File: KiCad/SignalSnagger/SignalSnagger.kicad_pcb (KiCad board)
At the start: 4 copper layers, 133.4 x 44.3 mm, 180 parts, among them J102 Left, J104 Right, J105 36-5005-ND, J106 36-5006-ND, J107 36-5006-ND, J108 36-5005-ND, J109 36-5006-ND, J110 36-5006-ND, J203 Conn_01x02, J204 Conn_01x02, J301 35RASMT2BHSNTRX, J302 36-5005-ND, J303 36-5005-ND, J304 36-5006-ND, P201 ISP/PDI, Q101 MMBT2222A, Q102 MMBT2222A, Q103 MMBT2222A, Q104 MMBT2222A, Q105 MMBT2222A, Q201 BSS84W-7-F, Q202 BSS138W-7-F, SW201 SW_SPST, SW202 SW_SPST, SW203 PEC12R-4225F-S0024, T101 Transformer_1P_SS, U102 QS3253QG8, U103 REF4132B33, U104 DG9422E, U105 DG9422E, U201 AVR128DA48, U202 SI5351, U203 LP2985-5.0, U204 LP2985-3.3, U205 EA_DOGS104W-A, U206 LP2985-5.0, U207 MAX1683EUK, U302 TS912IDT, U303 TS912IDT, U304 LM386, X201 ECS-327TXO-30-TR, X202 25 MHz

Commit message: Ver 0.307
PCB updates
o All components are now placed onto the board with not traces drawn
 oRe-added the stereo channel. Parts are numbered starting with 901, so they can be easily identified for not populating or future removal
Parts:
- removed U303: TS912IDT, Package_SO:SO-8_3.9x4.9mm_P1.27mm
- added C901: 150nF, Capacitor_SMD:C_0603_1608Metric, F.Cu at (166.2, 97.8)
- added C902: 4.7nF, Capacitor_SMD:C_0603_1608Metric, F.Cu at (161.8, 96.0)
- added C903: 100nF, Capacitor_SMD:C_0603_1608Metric, F.Cu at (161.8, 97.5)
- added C906: 10nF, Capacitor_SMD:C_0603_1608Metric, F.Cu at (201.4, 107.2)
- added C907: 47uF, Capacitor_SMD:C_1210_3225Metric, F.Cu at (200.6, 101.1)
- added C908: 1uF, Capacitor_SMD:C_0603_1608Metric, F.Cu at (202.2, 109.7)
- added C909: 100nF, Capacitor_SMD:C_0603_1608Metric, F.Cu at (201.2, 103.6)
- added C910: 10uF, Capacitor_SMD:C_0603_1608Metric, F.Cu at (201.4, 105.7)
- added C911: 100nF, Capacitor_SMD:C_0603_1608Metric, F.Cu at (209.2, 103.2)
- added C912: 22uF, Capacitor_SMD:C_0805_2012Metric, F.Cu at (208.3, 100.6)
- added R901: 4.7k, Resistor_SMD:R_0603_1608Metric, F.Cu at (169.3, 96.4)
- added R902: 7.5k, Resistor_SMD:R_0603_1608Metric, F.Cu at (167.7, 97.9)
- added R903: 51k, Resistor_SMD:R_0603_1608Metric, F.Cu at (157.0, 99.7)
- added R907: 10k, Resistor_SMD:R_0603_1608Metric, F.Cu at (196.5, 106.9)
- added R909: 10, Resistor_SMD:R_0603_1608Metric, F.Cu at (198.2, 103.5)
- added R910: 470, Resistor_SMD:R_0603_1608Metric, F.Cu at (200.6, 109.7)
- added R911: 10, Resistor_SMD:R_0603_1608Metric, F.Cu at (209.2, 106.3)
- added RV901: 100k, Potentiometer_SMD:Potentiometer_Bourns_TC33X_Vertical, F.Cu at (189.0, 105.3)
- added TP901: Conn_01x03, Connector_PinHeader_2.54mm:PinHeader_1x03_P2.54mm_Vertical, F.Cu at (192.8, 102.0)
- added U901: TS912IDT, Package_SO:SO-8_3.9x4.9mm_P1.27mm, F.Cu at (155.8, 94.8)
- added U902: LM386, Package_SO:SO-8_3.9x4.9mm_P1.27mm, F.Cu at (205.7, 106.4)
- JP103, JP104, JP105, JP106, JP107: footprint Jumper:Jumper_THT_1x02_P1.27mm_Vertical -> Jumper:Jumper_THT-1x02_Bridged_Circular
- moved R205 87.1 mm to (184.4, 85.4)
- moved J204 85.9 mm to (187.8, 84.7), turned to 180 degrees
- moved D204 85.5 mm to (191.4, 85.2)
- moved D203 84.7 mm to (191.3, 79.4)
- moved R204 83.9 mm to (184.1, 83.7)
- moved C202 83.9 mm to (168.8, 85.2)
- moved C217 83.9 mm to (167.4, 80.7)
- moved U201 83.9 mm to (175.6, 85.5)
- moved X201 83.9 mm to (172.9, 77.7)
- moved C213 83.9 mm to (176.8, 78.5)
- moved C214 83.9 mm to (184.0, 81.0)
- moved C221 83.9 mm to (170.1, 77.2)
- moved L201 83.9 mm to (180.7, 79.3)
- moved R209 83.9 mm to (180.9, 81.0)
- moved C203 83.9 mm to (178.4, 78.5)
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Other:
- board text added: "Sense Adjust"
- board text removed: "JP105"
- board text removed: "Sense"

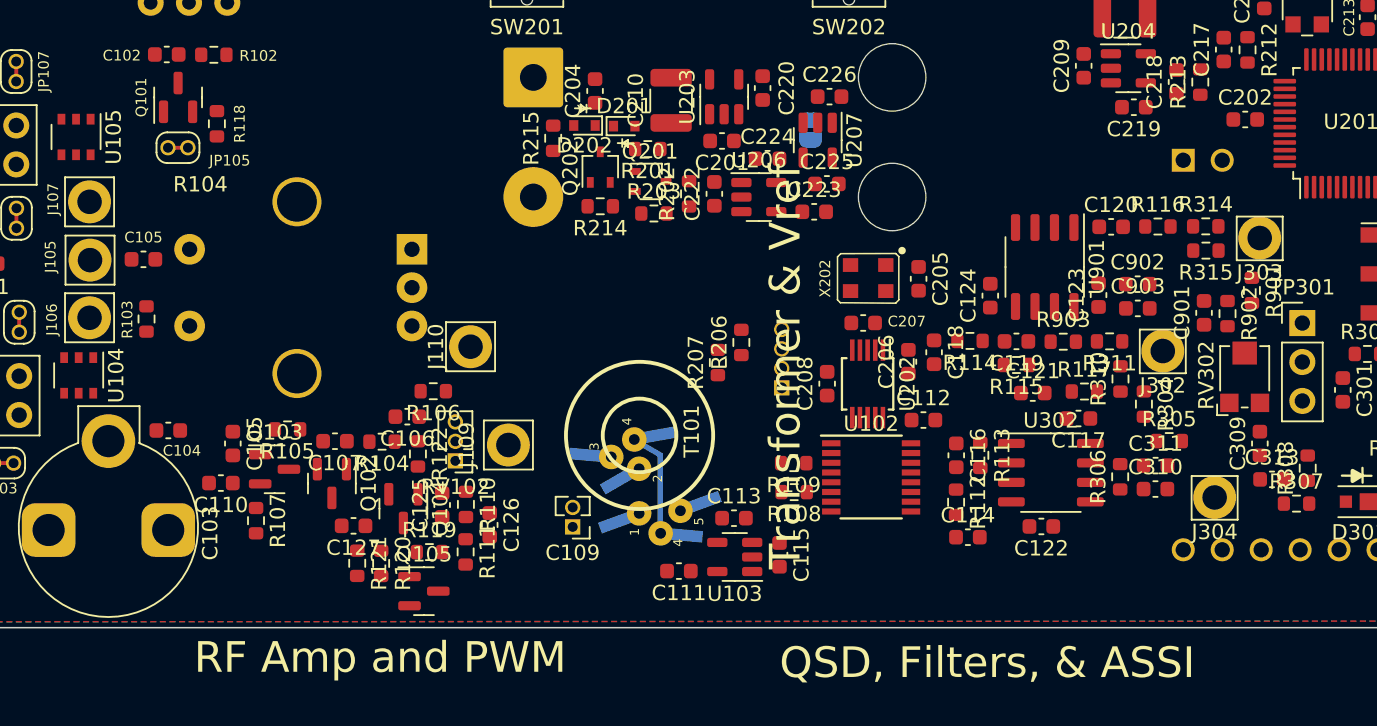
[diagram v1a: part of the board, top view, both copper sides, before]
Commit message: Ver 0.308
Schematic and PCB tweaks
Set board thickness to 1.6mm
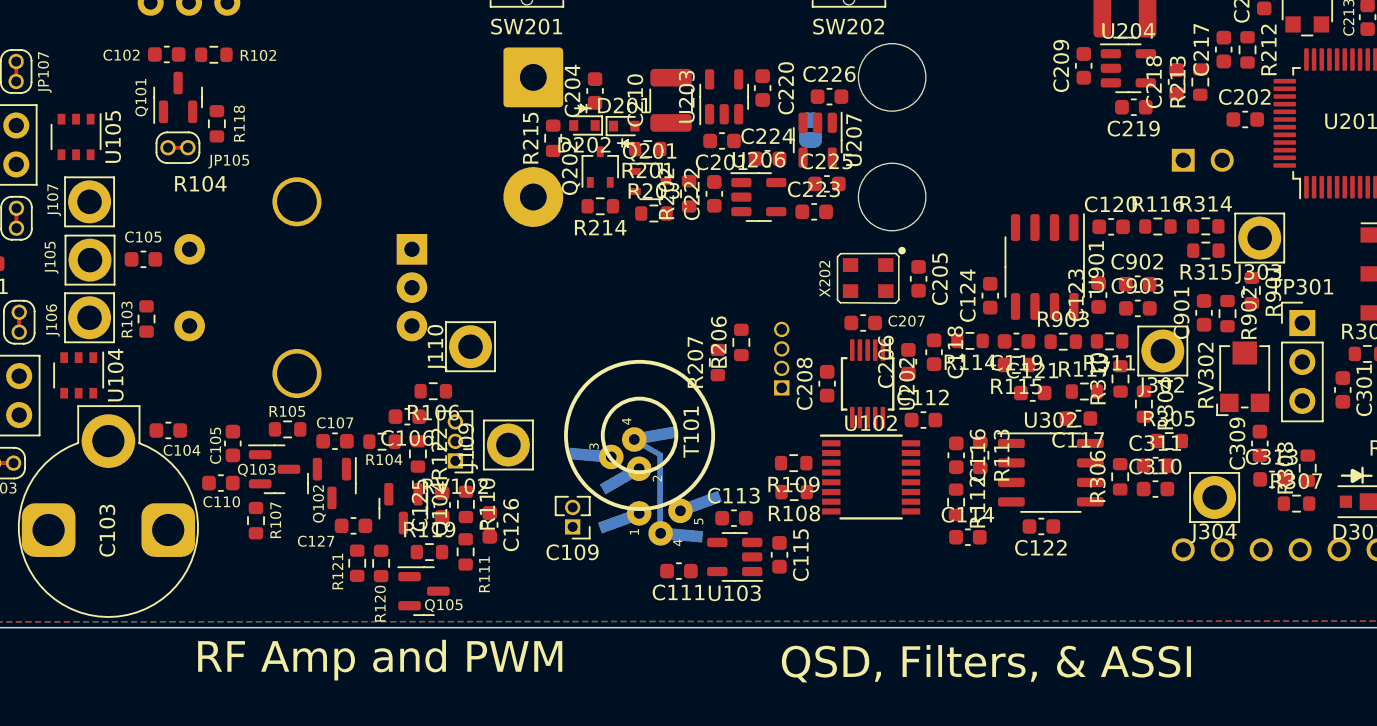
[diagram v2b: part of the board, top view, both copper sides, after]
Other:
- board text removed: "Transformer & Vref"

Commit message: Ver 0.309
PCB layout updates
Schematic updates
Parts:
- removed J303: 36-5005-ND, Connector_Pin:Pin_D1.6mm_L8.5mm_W2.8mm_FlatFork
- removed R116: 100, Resistor_SMD:R_0603_1608Metric
- added C108: 100nF, Capacitor_SMD:C_0603_1608Metric, F.Cu at (92.2, 88.8)
- added C118: 100nF, Capacitor_SMD:C_0603_1608Metric, F.Cu at (92.3, 103.2)
- added J218: Conn_01x02, Connector_PinSocket_1.27mm:PinSocket_1x02_P1.27mm_Vertical, F.Cu at (127.9, 75.5)
- added J219: Conn_01x02, Connector_PinSocket_1.27mm:PinSocket_1x02_P1.27mm_Vertical, F.Cu at (148.9, 75.5)
- added J220: Conn_01x02, Connector_PinSocket_1.27mm:PinSocket_1x02_P1.27mm_Vertical, F.Cu at (127.9, 115.5)
- added J221: Conn_01x02, Connector_PinSocket_1.27mm:PinSocket_1x02_P1.27mm_Vertical, F.Cu at (148.9, 115.4)
- added J903: 36-5005-ND, Connector_Pin:Pin_D1.6mm_L8.5mm_W2.8mm_FlatFork, F.Cu at (161.8, 105.6)
- added R916: 100, Resistor_SMD:R_0603_1608Metric, F.Cu at (156.9, 103.9)
- added SW204: SW_SPST, Button_Switch_SMD:SW_SPST_TL1014BF160QG, F.Cu at (122.1, 116.4)
- added SW205: SW_SPST, Button_Switch_SMD:SW_SPST_TL1014BF160QG, F.Cu at (143.1, 116.3)
- C103: moved to B.Cu
- C109: footprint Connector_PinHeader_1.27mm:PinHeader_1x02_P1.27mm_Vertical -> Capacitor_SMD:C_0603_1608Metric
- J102: renamed from J104; value Right -> Left; moved to B.Cu
- J104: renamed from J102; value Left -> Right; moved to B.Cu
- R930: renamed from R315; value 10k -> 49.9k
- R931: renamed from R314; value 49.9k -> 10k
- moved R207 26.4 mm to (154.7, 84.2), turned to 180 degrees
- moved R206 25.2 mm to (157.0, 86.0), turned to -90 degrees
- moved R915 24.7 mm to (131.2, 110.9), turned to 90 degrees
- moved C919 24.0 mm to (132.7, 110.9), turned to 90 degrees
- moved J302 23.0 mm to (140.9, 95.9)
- moved C918 21.0 mm to (128.9, 107.6), turned to 180 degrees
- moved R914 20.6 mm to (131.9, 107.6)
- moved TP201 20.3 mm to (151.3, 86.9), turned to -90 degrees
- moved JP107 20.0 mm to (81.2, 100.6)
- moved R305 19.6 mm to (146.8, 96.7), turned to 180 degrees
- moved U105 19.5 mm to (92.1, 105.8)
- moved C924 18.5 mm to (142.5, 112.4), turned to -90 degrees
- moved C901 18.2 mm to (153.2, 110.6)
- moved JP106 18.2 mm to (88.5, 109.8), turned to 180 degrees
- moved R108 18.1 mm to (121.4, 108.5)
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- renumbered C118 to C918, C119 to C919, C120 to C920, C123 to C923, C124 to C924, R114 to R914, R115 to R915
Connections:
- J102 pad 1: Net-(J102-Pad2) -> Net-(C103-Pad1)
- J102 pad 2: Net-(J102-Pad3) -> Net-(J102-Pad2)
- J102 pad 3: GND -> Net-(J102-Pad3)
- J102 pad 4: Net-(J102-Pad5) -> GND
- J102 pad 5: Net-(J102-Pad6) -> Net-(J102-Pad5)
- J102 pad 6: Net-(C103-Pad2) -> Net-(J102-Pad6)
- J102 pad 7: Net-(J104-Pad7) -> Net-(J102-Pad7)
- J102 pad 8: Net-(J104-Pad8) -> Net-(J102-Pad8)
- J104 pad 1: Net-(C103-Pad1) -> Net-(J102-Pad2)
- J104 pad 2: Net-(J102-Pad2) -> Net-(J102-Pad3)
- J104 pad 3: Net-(J102-Pad3) -> GND
- J104 pad 4: GND -> Net-(J102-Pad5)
- J104 pad 5: Net-(J102-Pad5) -> Net-(J102-Pad6)
- J104 pad 6: Net-(J102-Pad6) -> Net-(C103-Pad2)
- J104 pad 7: Net-(J102-Pad7) -> Net-(J104-Pad7)
- J104 pad 8: Net-(J102-Pad8) -> Net-(J104-Pad8)
- R930 pad 1: Audio I -> I OUT
- R930 pad 2: GND -> Audio I
- R931 pad 1: I OUT -> Audio I
- R931 pad 2: Audio I -> GND
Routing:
- net GND: track 0.00 -> 16.3 mm
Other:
- board text added: "KT-70 Plastic Electronics Enclosure 5.50 x 2.00 x 0.80 in / 140 x 51 x 20 mm / 0.13 lbs"

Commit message: Ver 0.310
Schematic and PCB updates
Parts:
- added JP202: Jumper_2_Bridged, Jumper:Jumper_THT-1x02_Bridged_Circular, F.Cu at (193.0, 72.6)
- J108, JP103, JP104, JP106, JP107: moved to B.Cu
- moved TP901 33.4 mm to (160.6, 110.9)
- moved RV901 33.3 mm to (156.8, 114.0)
- moved C301 13.7 mm to (163.3, 96.0)
- moved RV302 13.7 mm to (156.9, 95.0)
- moved C313 13.7 mm to (158.7, 101.8)
- moved C314 13.7 mm to (167.4, 98.7)
- moved D301 13.7 mm to (164.4, 103.2)
- moved R309 13.7 mm to (169.0, 98.7)
- moved R303 13.7 mm to (165.0, 93.6)
- moved R313 13.7 mm to (166.8, 101.2)
- moved TP301 13.7 mm to (160.7, 91.6)
- moved C309 13.7 mm to (157.9, 99.5)
- moved R307 13.7 mm to (160.3, 103.4)
- moved R308 13.7 mm to (161.1, 101.1)
- moved JP107 12.2 mm to (88.9, 110.2), turned to 90 degrees
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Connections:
- C202 pad 1: GND -> GNDD
- C203 pad 1: GND -> GNDD
- C205 pad 1: GND -> GNDD
- C206 pad 1: GND -> GNDD
- C208 pad 2: GND -> GNDD
- C209 pad 1: GND -> GNDD
- C211 pad 1: GND -> GNDD
- C212 pad 1: GND -> GNDD
- C213 pad 2: GND -> GNDD
- C214 pad 2: GND -> GNDD
- C215 pad 2: GND -> GNDD
- C216 pad 1: GND -> GNDD
- C217 pad 2: GND -> GNDD
- C218 pad 1: GND -> GNDD
- C219 pad 2: GND -> GNDD
- C221 pad 1: GND -> GNDD
- D203 pad 1: GND -> GNDD
- D204 pad 1: GND -> GNDD
- J203 pad 1: GND -> GNDD
- J204 pad 1: GND -> GNDD
- J218 pad 1: GND -> GNDD
- J219 pad 1: GND -> GNDD
- P201 pad 6: GND -> GNDD
- SW201 pad 2: GND -> GNDD
- SW202 pad 2: GND -> GNDD
- SW203 pad C: GND -> GNDD
- SW203 pad S2: GND -> GNDD
- TP201 pad 1: GND -> GNDD
- U201 pad 15: GND -> GNDD
- U201 pad 29: GND -> GNDD
- U201 pad 43: GND -> GNDD
- U202 pad 8: GND -> GNDD
- U204 pad 2: GND -> GNDD
- U205 pad 12: GND -> GNDD
- U205 pad 14: GND -> GNDD
- U205 pad 18: GND -> GNDD
- U205 pad 19: GND -> GNDD
- X201 pad 2: GND -> GNDD
- X202 pad 2: GND -> GNDD
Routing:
- net GNDD: track 0.00 -> 16.3 mm
- net GND: track 16.3 -> 0.00 mm
- added copper zone on F.Cu, net GND
- added copper zone on F.Cu, net GNDD
- removed copper zone on F.Cu, net Net-(J102-Pad8)
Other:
- board text added: "LEFT"
- board text added: "RIGHT"
